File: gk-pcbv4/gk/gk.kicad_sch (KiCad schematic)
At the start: 19 parts

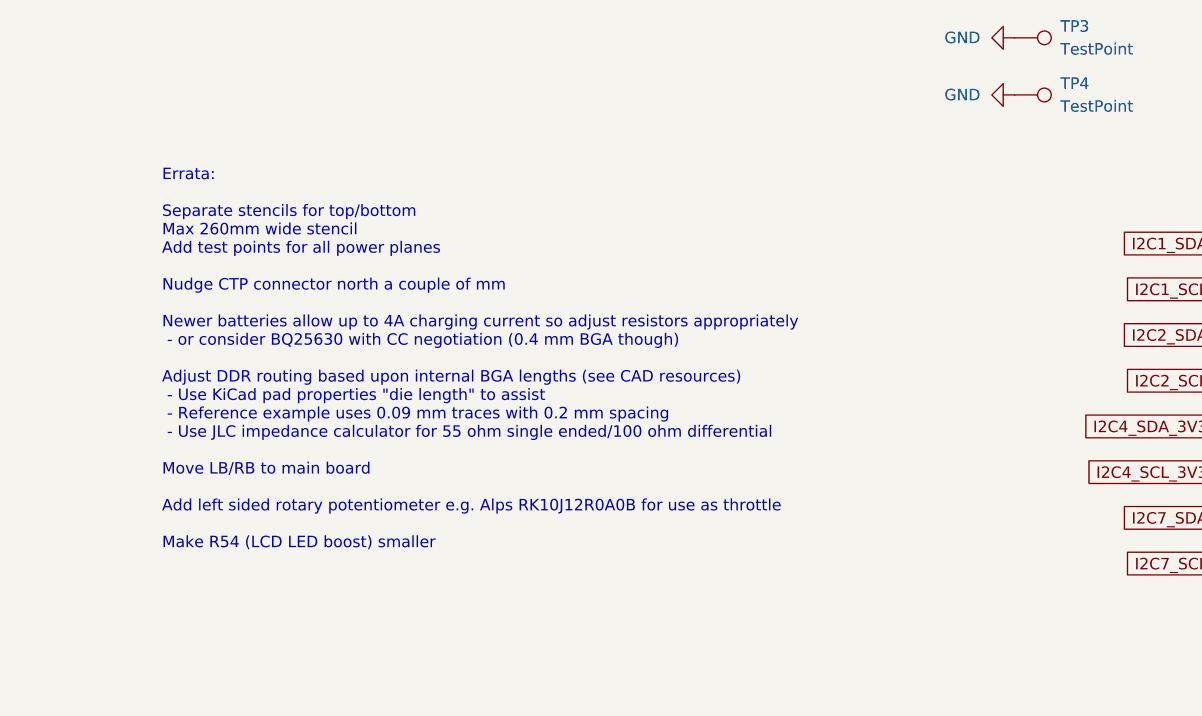
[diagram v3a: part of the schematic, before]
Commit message: add test points to power planes
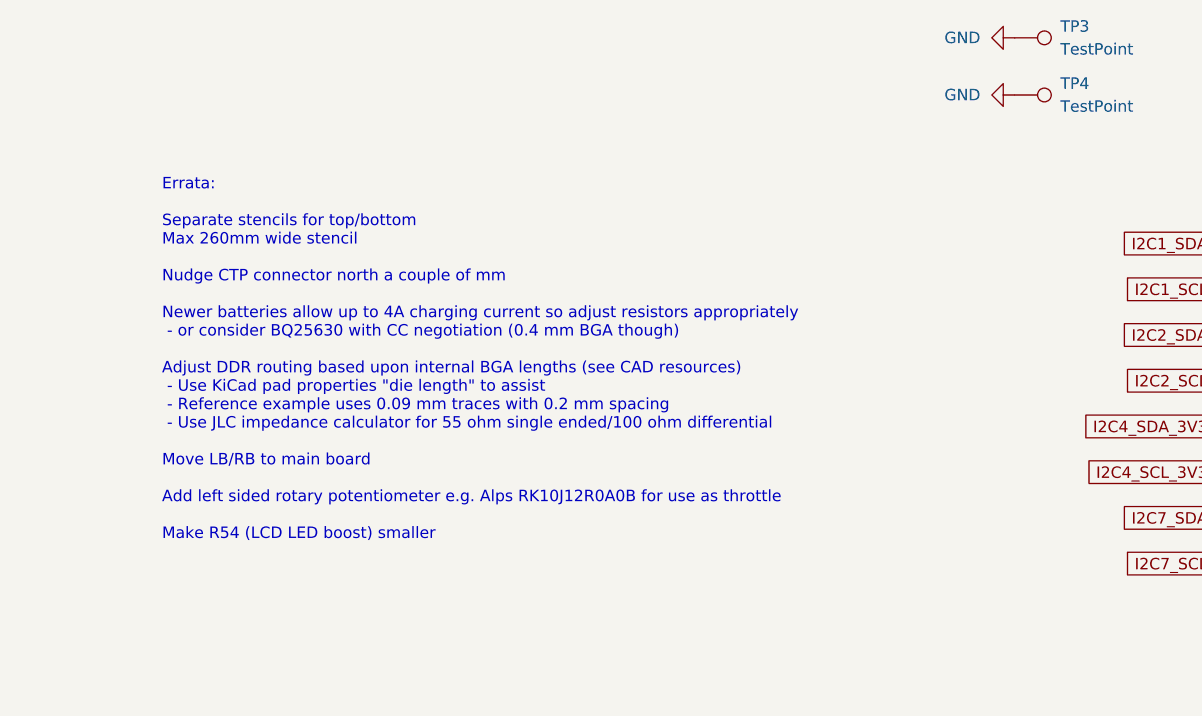
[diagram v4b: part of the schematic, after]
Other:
- note added: "Errata: Separate stencils for top/bottom Max 260mm wide stencil Nudge CTP connector north a couple of mm Newer batteries allow up to 4A charging current so adjust resistors appropriately - or consider BQ25630 with CC negotiation (0.4 mm BGA though) Adjust DDR routing based upon internal BGA lengths (see CAD resources) - Use KiCad pad properties "die length" to assist - Reference example uses 0.09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"
- note removed: "Errata: Separate stencils for top/bottom Max 260mm wide stencil Add test points for all power planes Nudge CTP connector north a couple of mm Newer batteries allow up to 4A charging current so adjust resistors appropriately - or consider BQ25630 with CC negotiation (0.4 mm BGA though) Adjust DDR routing based upon internal BGA lengths (see CAD resources) - Use KiCad pad properties "die length" to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"
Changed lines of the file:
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@@
 		)
 	)
-	(text "Errata:\n\nSeparate stencils for top/bottom\nMax 260mm wide stencil\nAdd test points for all power planes\n\nNudge CTP connector north a couple of mm\n\nNewer batteries allow up to 4A charging current so adjust resistors appropriately\n - or consider BQ25630 with CC negotiation (0.4 mm BGA though)\n\nAdjust DDR routing based upon internal BGA lengths (see CAD resources)\n - Use KiCad pad properties \"die length\" to assist\n - Reference example uses 0.09 mm traces with 0.2 mm spacing\n - Use JLC impedance calculator for 55 ohm single ended/100 ohm differential\n\nMove LB/RB to main board\n\nAdd left sided rotary potentiometer e.g. Alps RK10J12R0A0B for use as throttle\n\nMake R54 (LCD LED boost) smaller\n\n"
+	(text "Errata:\n\nSeparate stencils for top/bottom\nMax 260mm wide stencil\n\nNudge CTP connector north a couple of mm\n\nNewer batteries allow up to 4A charging current so adjust resistors appropriately\n - or consider BQ25630 with CC negotiation (0.4 mm BGA though)\n\nAdjust DDR routing based upon internal BGA lengths (see CAD resources)\n - Use KiCad pad properties \"die length\" to assist\n - Reference example uses 0.09 mm traces with 0.2 mm spacing\n - Use JLC impedance calculator for 55 ohm single ended/100 ohm differential\n\nMove LB/RB to main board\n\nAdd left sided rotary potentiometer e.g. Alps RK10J12R0A0B for use as throttle\n\nMake R54 (LCD LED boost) smaller\n\n"
 		(exclude_from_sim no)
 		(at 104.648 80.01 0)

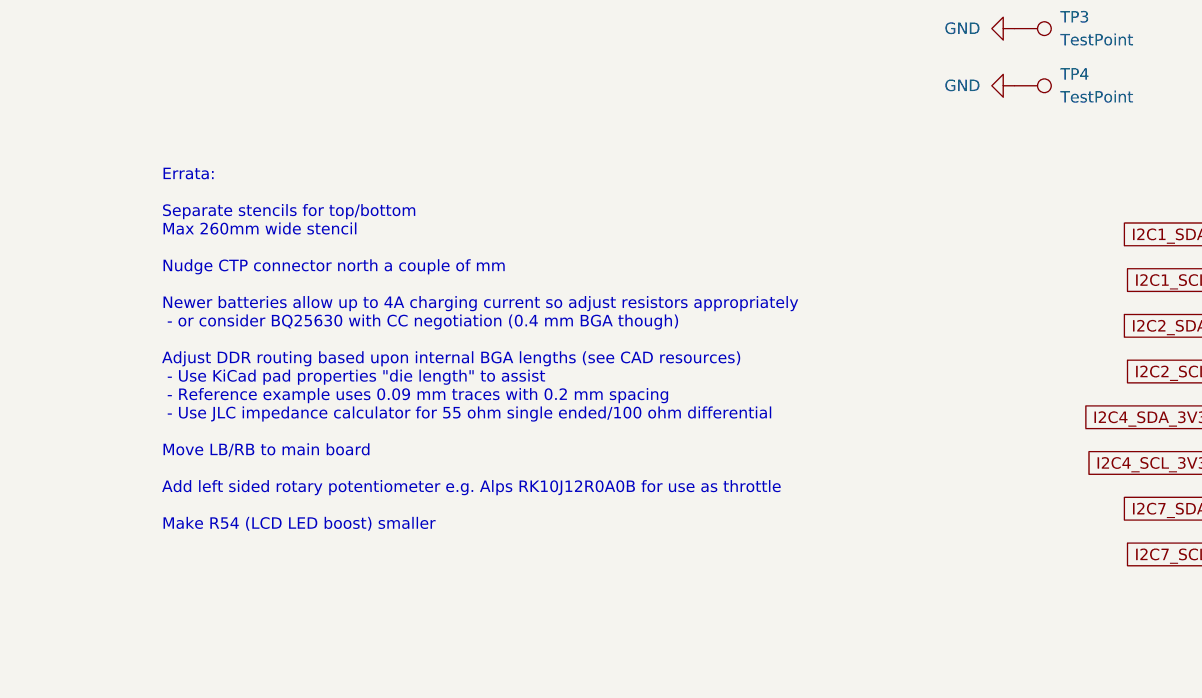
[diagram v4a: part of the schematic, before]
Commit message: move ctp connector north 2 mm
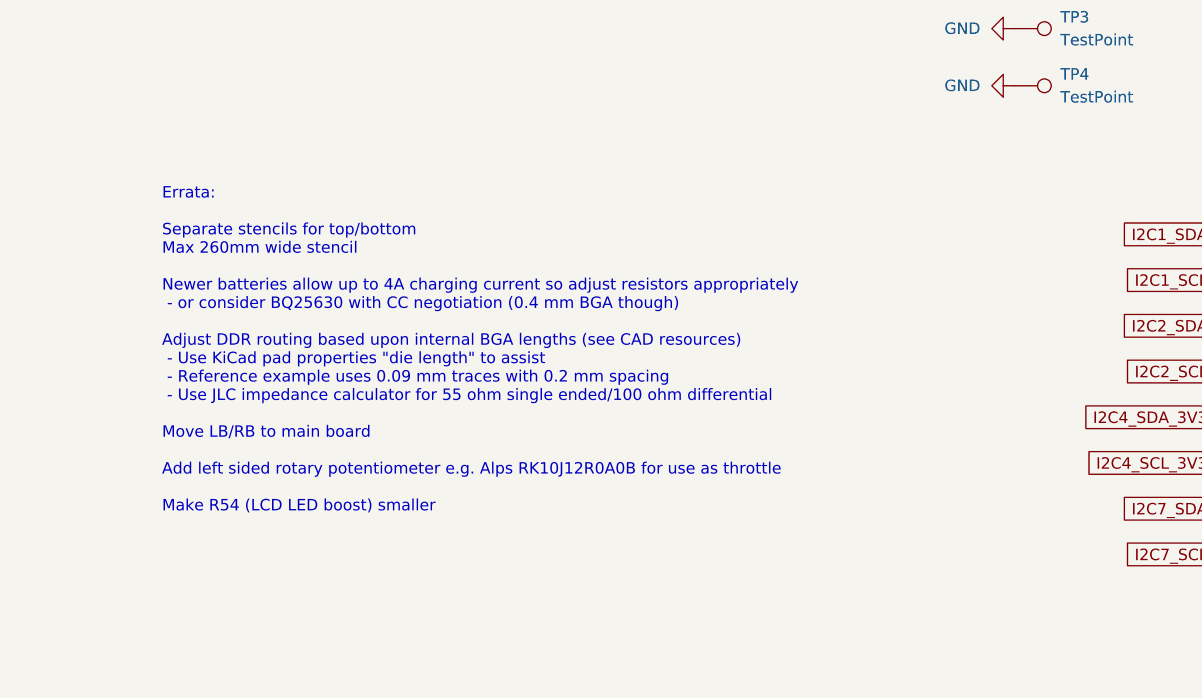
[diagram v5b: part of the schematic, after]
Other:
- note added: "Errata: Separate stencils for top/bottom Max 260mm wide stencil Newer batteries allow up to 4A charging current so adjust resistors appropriately - or consider BQ25630 with CC negotiation (0.4 mm BGA though) Adjust DDR routing based upon internal BGA lengths (see CAD resources) - Use KiCad pad properties "die length" to assist - Reference example uses 0.09 mm traces with 0.2 mm spacing - Use JLC 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"
- note removed: "Errata: Separate stencils for top/bottom Max 260mm wide stencil Nudge CTP connector north a couple of mm Newer batteries allow up to 4A charging current so adjust resistors appropriately - or consider BQ25630 with CC negotiation (0.4 mm BGA though) Adjust DDR routing based upon internal BGA lengths (see CAD resources) - Use KiCad pad properties "die length" to assist - Reference example uses 0.09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"
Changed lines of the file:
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@@
 		)
 	)
-	(text "Errata:\n\nSeparate stencils for top/bottom\nMax 260mm wide stencil\n\nNudge CTP connector north a couple of mm\n\nNewer batteries allow up to 4A charging current so adjust resistors appropriately\n - or consider BQ25630 with CC negotiation (0.4 mm BGA though)\n\nAdjust DDR routing based upon internal BGA lengths (see CAD resources)\n - Use KiCad pad properties \"die length\" to assist\n - Reference example uses 0.09 mm traces with 0.2 mm spacing\n - Use JLC impedance calculator for 55 ohm single ended/100 ohm differential\n\nMove LB/RB to main board\n\nAdd left sided rotary potentiometer e.g. Alps RK10J12R0A0B for use as throttle\n\nMake R54 (LCD LED boost) smaller\n\n"
+	(text "Errata:\n\nSeparate stencils for top/bottom\nMax 260mm wide stencil\n\nNewer batteries allow up to 4A charging current so adjust resistors appropriately\n - or consider BQ25630 with CC negotiation (0.4 mm BGA though)\n\nAdjust DDR routing based upon internal BGA lengths (see CAD resources)\n - Use KiCad pad properties \"die length\" to assist\n - Reference example uses 0.09 mm traces with 0.2 mm spacing\n - Use JLC impedance calculator for 55 ohm single ended/100 ohm differential\n\nMove LB/RB to main board\n\nAdd left sided rotary potentiometer e.g. Alps RK10J12R0A0B for use as throttle\n\nMake R54 (LCD LED boost) smaller\n\n"
 		(exclude_from_sim no)
 		(at 104.648 80.01 0)

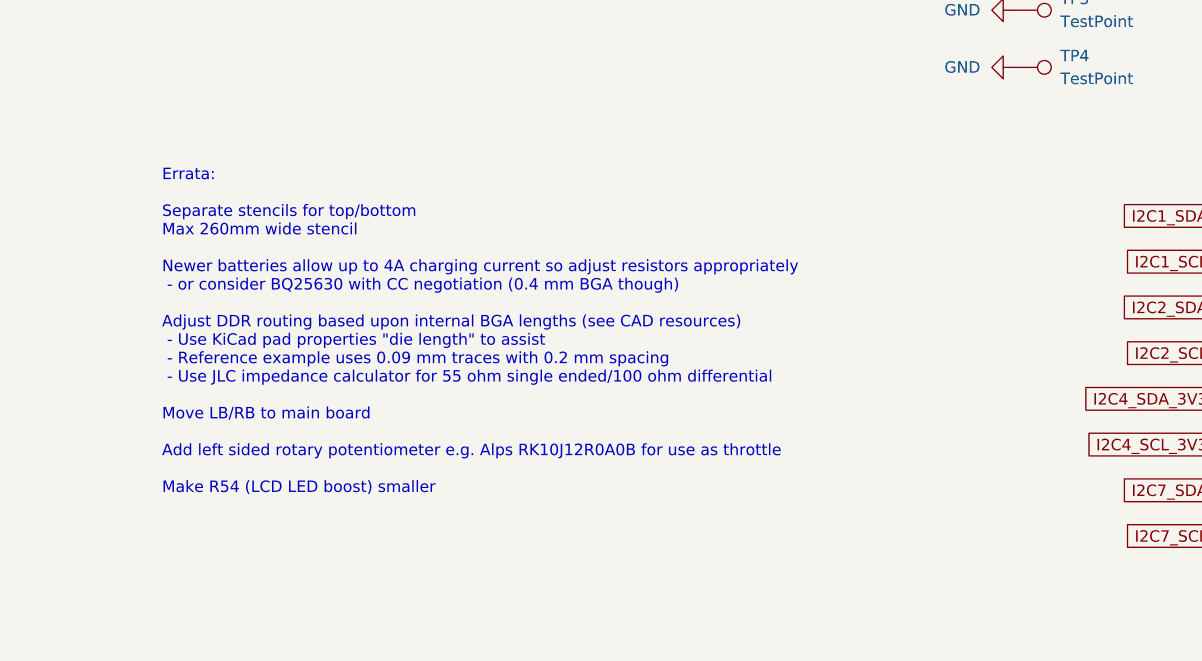
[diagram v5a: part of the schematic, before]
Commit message: add bq25601 battery charger as alternative
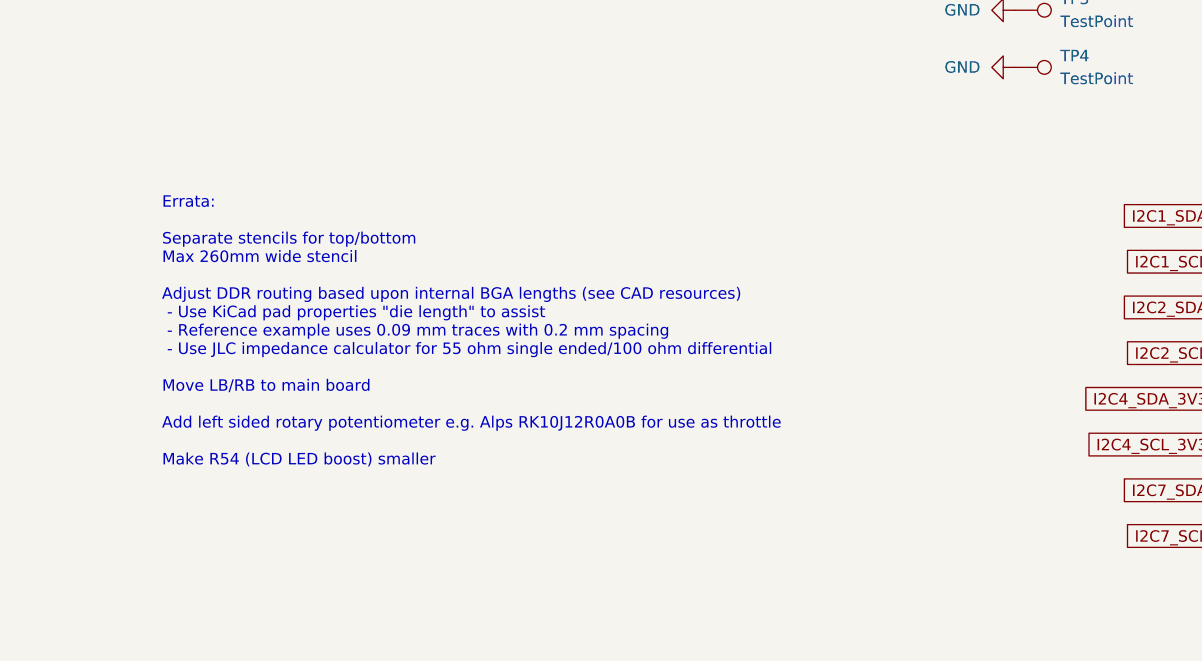
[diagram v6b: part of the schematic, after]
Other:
- note added: "Errata: Separate stencils for top/bottom Max 260mm wide stencil Adjust DDR routing based upon internal BGA lengths (see CAD resources) - Use KiCad pad properties "die length" to assist - Reference example uses 0.09 mm traces with 0.2 mm spacing - Use JLC impedance calculator for 55 ohm single ended/100 ohm differential Move LB/RB to main board Add left sided rotary potentiometer e.g. Alps RK10J12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"
- note removed: "Errata: Separate stencils for top/bottom Max 260mm wide stencil Newer batteries allow up to 4A charging current so adjust resistors appropriately - or consider BQ25630 with CC negotiation (0.4 mm BGA though) Adjust DDR routing based upon internal BGA lengths (see CAD resources) - Use KiCad pad properties "die length" to assist - Reference example uses 0.09 mm traces with 0.2 mm spacing - Use JLC 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"
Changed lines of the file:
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@@
 		)
 	)
-	(text "Errata:\n\nSeparate stencils for top/bottom\nMax 260mm wide stencil\n\nNewer batteries allow up to 4A charging current so adjust resistors appropriately\n - or consider BQ25630 with CC negotiation (0.4 mm BGA though)\n\nAdjust DDR routing based upon internal BGA lengths (see CAD resources)\n - Use KiCad pad properties \"die length\" to assist\n - Reference example uses 0.09 mm traces with 0.2 mm spacing\n - Use JLC impedance calculator for 55 ohm single ended/100 ohm differential\n\nMove LB/RB to main board\n\nAdd left sided rotary potentiometer e.g. Alps RK10J12R0A0B for use as throttle\n\nMake R54 (LCD LED boost) smaller\n\n"
+	(text "Errata:\n\nSeparate stencils for top/bottom\nMax 260mm wide stencil\n\nAdjust DDR routing based upon internal BGA lengths (see CAD resources)\n - Use KiCad pad properties \"die length\" to assist\n - Reference example uses 0.09 mm traces with 0.2 mm spacing\n - Use JLC impedance calculator for 55 ohm single ended/100 ohm differential\n\nMove LB/RB to main board\n\nAdd left sided rotary potentiometer e.g. Alps RK10J12R0A0B for use as throttle\n\nMake R54 (LCD LED boost) smaller\n\n"
 		(exclude_from_sim no)
 		(at 104.648 80.01 0)

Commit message: Add throttle control
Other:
- note added: "Errata: Separate stencils for top/bottom Max 260mm wide stencil Adjust DDR routing based upon internal BGA lengths (see CAD resources) - Use KiCad pad properties "die length" to assist - Reference example uses 0.09 mm traces with 0.2 mm spacing - Use JLC impedance calculator for 55 ohm single ended/100 ohm differential Move LB/RB to main board Make R54 (LCD LED boost) smaller"
- note removed: "Errata: Separate stencils for top/bottom Max 260mm wide stencil Adjust DDR routing based upon internal BGA lengths (see CAD resources) - Use KiCad pad properties "die length" to assist - Reference example uses 0.09 mm traces with 0.2 mm spacing - Use JLC impedance calculator for 55 ohm single ended/100 ohm differential Move LB/RB to main board Add left sided rotary potentiometer e.g. Alps RK10J12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"
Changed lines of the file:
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@@
 		)
 	)
-	(text "Errata:\n\nSeparate stencils for top/bottom\nMax 260mm wide stencil\n\nAdjust DDR routing based upon internal BGA lengths (see CAD resources)\n - Use KiCad pad properties \"die length\" to assist\n - Reference example uses 0.09 mm traces with 0.2 mm spacing\n - Use JLC impedance calculator for 55 ohm single ended/100 ohm differential\n\nMove LB/RB to main board\n\nAdd left sided rotary potentiometer e.g. Alps RK10J12R0A0B for use as throttle\n\nMake R54 (LCD LED boost) smaller\n\n"
+	(text "Errata:\n\nSeparate stencils for top/bottom\nMax 260mm wide stencil\n\nAdjust DDR routing based upon internal BGA lengths (see CAD resources)\n - Use KiCad pad properties \"die length\" to assist\n - Reference example uses 0.09 mm traces with 0.2 mm spacing\n - Use JLC impedance calculator for 55 ohm single ended/100 ohm differential\n\nMove LB/RB to main board\n\nMake R54 (LCD LED boost) smaller\n\n"
 		(exclude_from_sim no)
 		(at 104.648 80.01 0)
